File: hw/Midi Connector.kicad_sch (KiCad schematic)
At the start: 18 parts, among them J2 Midi In, J3 Midi Out, J4 Midi Thru, U5 74HC14, U6 H11L1

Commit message: huge schematic rework
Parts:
- removed C21, C22: 100n, Capacitor_SMD:C_0603_1608Metric, symbol Device:C
- removed D3: 1N4148WS, Diode_SMD:D_SOD-323, symbol Diode:1N4148WS
- removed J2: Midi In, DIN5_MIDI_MultiGround:DIN5_MIDI_MultiGround, symbol Connector:DIN-5_180degree
- removed J4: Midi Thru, DIN5_MIDI_MultiGround:DIN5_MIDI_MultiGround, symbol Connector:DIN-5_180degree
- removed R10, R15, R16: 220, Resistor_SMD:R_0603_1608Metric, symbol Device:R
- removed R11, R12: 1k, Resistor_SMD:R_0603_1608Metric, symbol Device:R
- removed TP6: MIDI_RX, TestPoint:TestPoint_Pad_D2.0mm, symbol Connector:TestPoint
- removed U6: H11L1, SOP-6-2.54mm:SOP-6_6.35x8.51mm_P02.54mm, symbol Isolator:H11L1
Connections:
- net STM_USART1_RX is gone; now on net GND: U5.11
- net GND: now also U5.9
- net at U5.10: no longer U5.9
- no-connect marks 10 -> 7
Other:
- moved on the sheet: C20, J3, R13, R14, TP7, U5A, U5B, U5C, U5D, U5E, U5F, U5G

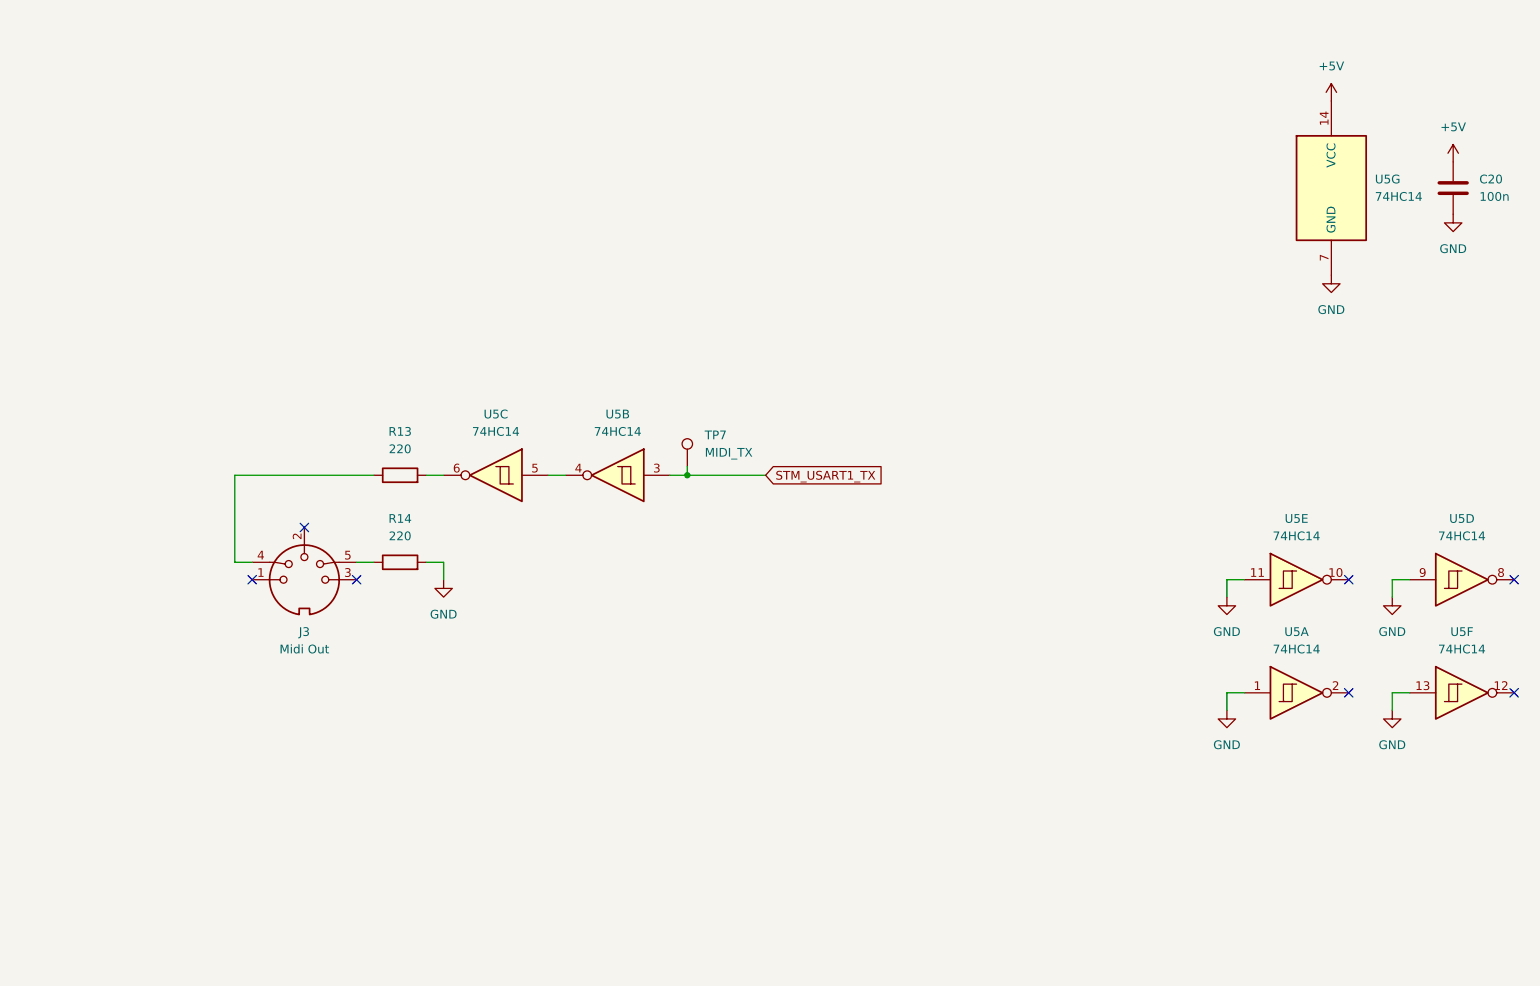
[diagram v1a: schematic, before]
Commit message: added new pcb design, ERC errors not fixed yet
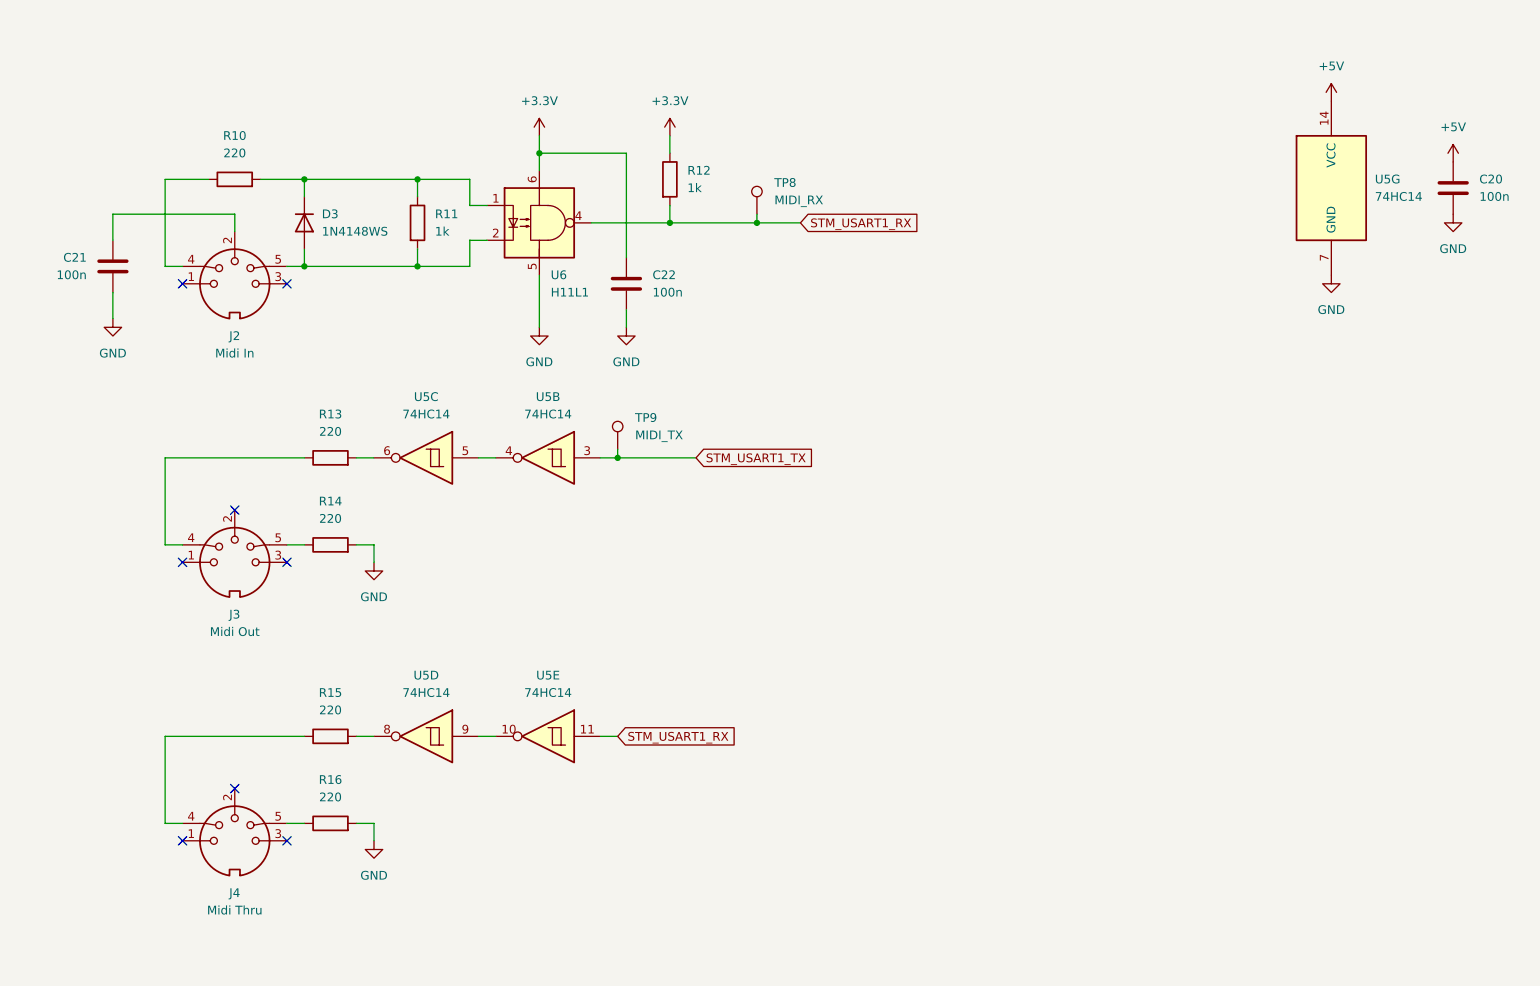
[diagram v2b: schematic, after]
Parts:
- removed unit 6 of U5
- removed unit 1 of U5
- added C21, C22: 100n, Capacitor_SMD:C_0603_1608Metric, symbol Device:C
- added D3: 1N4148WS, Diode_SMD:D_SOD-323, symbol Diode:1N4148WS
- added J2: Midi In, DIN5_MIDI_MultiGround:DIN5_MIDI_MultiGround, symbol Connector:DIN-5_180degree
- added J4: Midi Thru, DIN5_MIDI_MultiGround:DIN5_MIDI_MultiGround, symbol Connector:DIN-5_180degree
- added R10, R15, R16: 220, Resistor_SMD:R_0603_1608Metric, symbol Device:R
- added R11, R12: 1k, Resistor_SMD:R_0603_1608Metric, symbol Device:R
- added TP8: MIDI_RX, TestPoint:TestPoint_Pad_D2.0mm, symbol Connector:TestPoint
- added U6: H11L1, SOP-6-2.54mm:SOP-6_6.35x8.51mm_P02.54mm, symbol Isolator:H11L1
- renumbered TP7 to TP9
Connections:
- net GND: now also C21.2, C22.2, R16.2, U6.5; no longer U5.11, U5.9
- net at U5.8: now also R15.2
- net at U5.10: now also U5.9
- new net: J4.4, R15.1
- new net: J4.5, R16.1
- new net: D3.1 (K), R10.2, R11.1, U6.1
- new net: D3.2 (A), J2.5, R11.2, U6.2
- new net: C21.1, J2.2
- new net: J2.4, R10.1
- new net +3.3V: C22.1, R12.1, U6.6
- new net STM_USART1_RX: R12.2, TP8.1, U5.11, U6.4
- no-connect marks 7 -> 8
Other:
- moved on the sheet: J3, R13, R14, TP9, U5B, U5C

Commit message: updates to hardware layer
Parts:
- added C28: 100n, Capacitor_SMD:C_0603_1608Metric, symbol Device:C
- added unit 6 of U5
- added unit 1 of U5
- J2, J3, J4: symbol Connector:DIN-5_180degree -> Midi_Expressor:DIN-5_180degree_shielded
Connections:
- net GND: now also J3.S, J4.S, C28.2, U5.1, U5.13
- new net MIDI_IN_SHIELD: C28.1, J2.S
- no-connect marks 8 -> 10
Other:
- moved on the sheet: C21, C22, D3, R10, R11, R12, R13, R14, R15, R16, TP8, TP9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

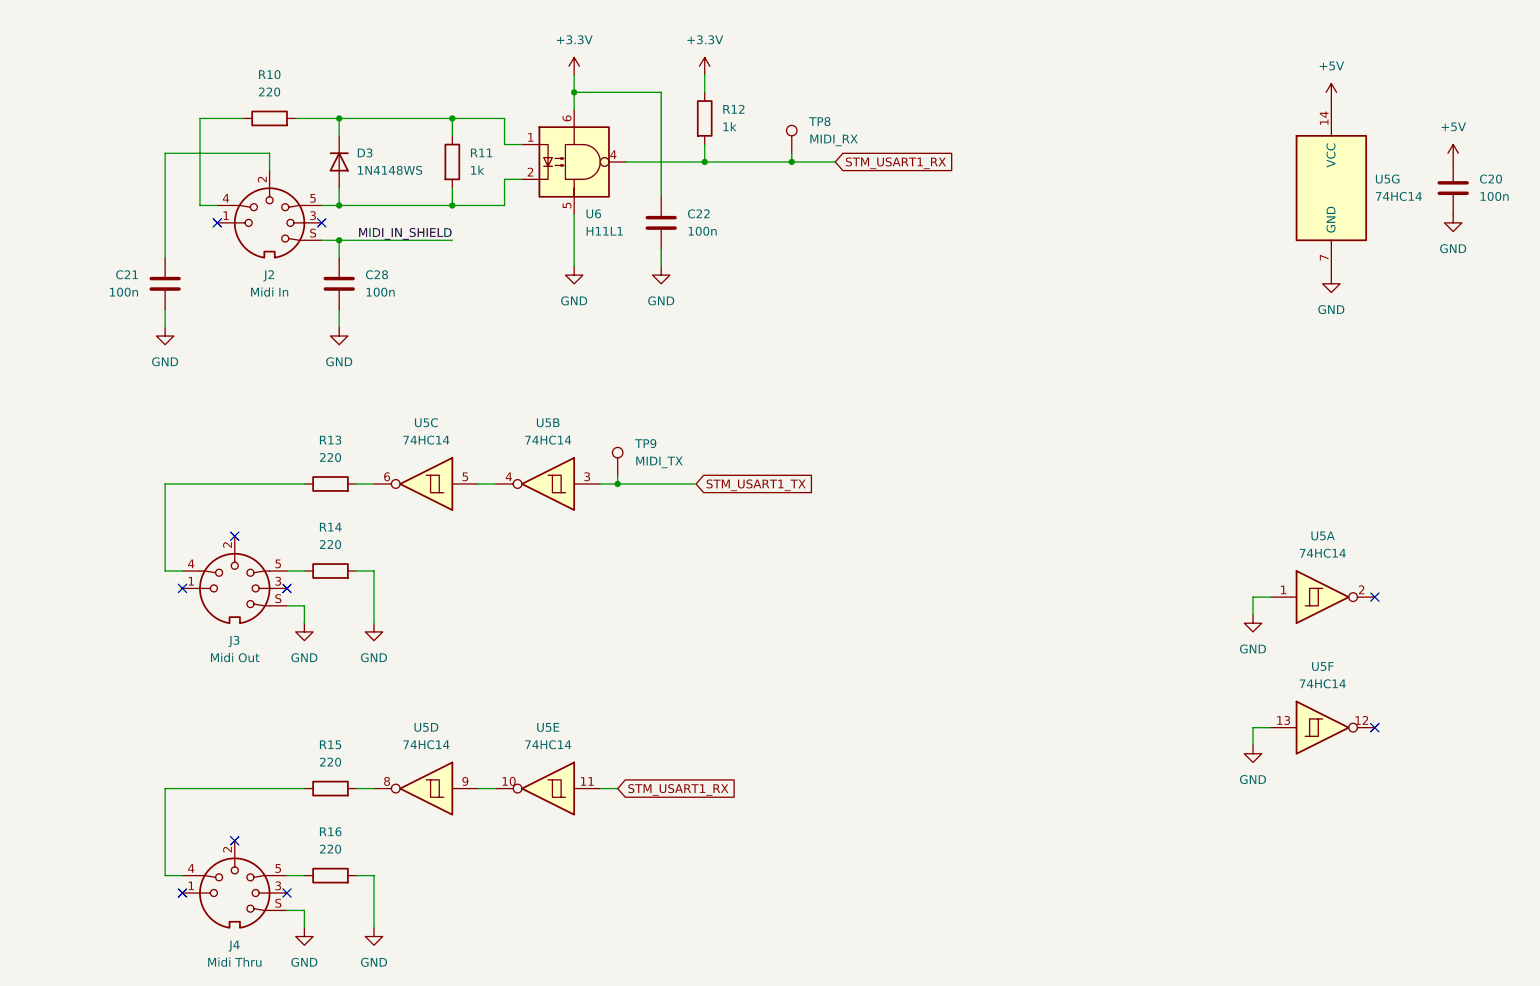
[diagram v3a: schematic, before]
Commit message: updated midi circuit to use 3.3V logic level
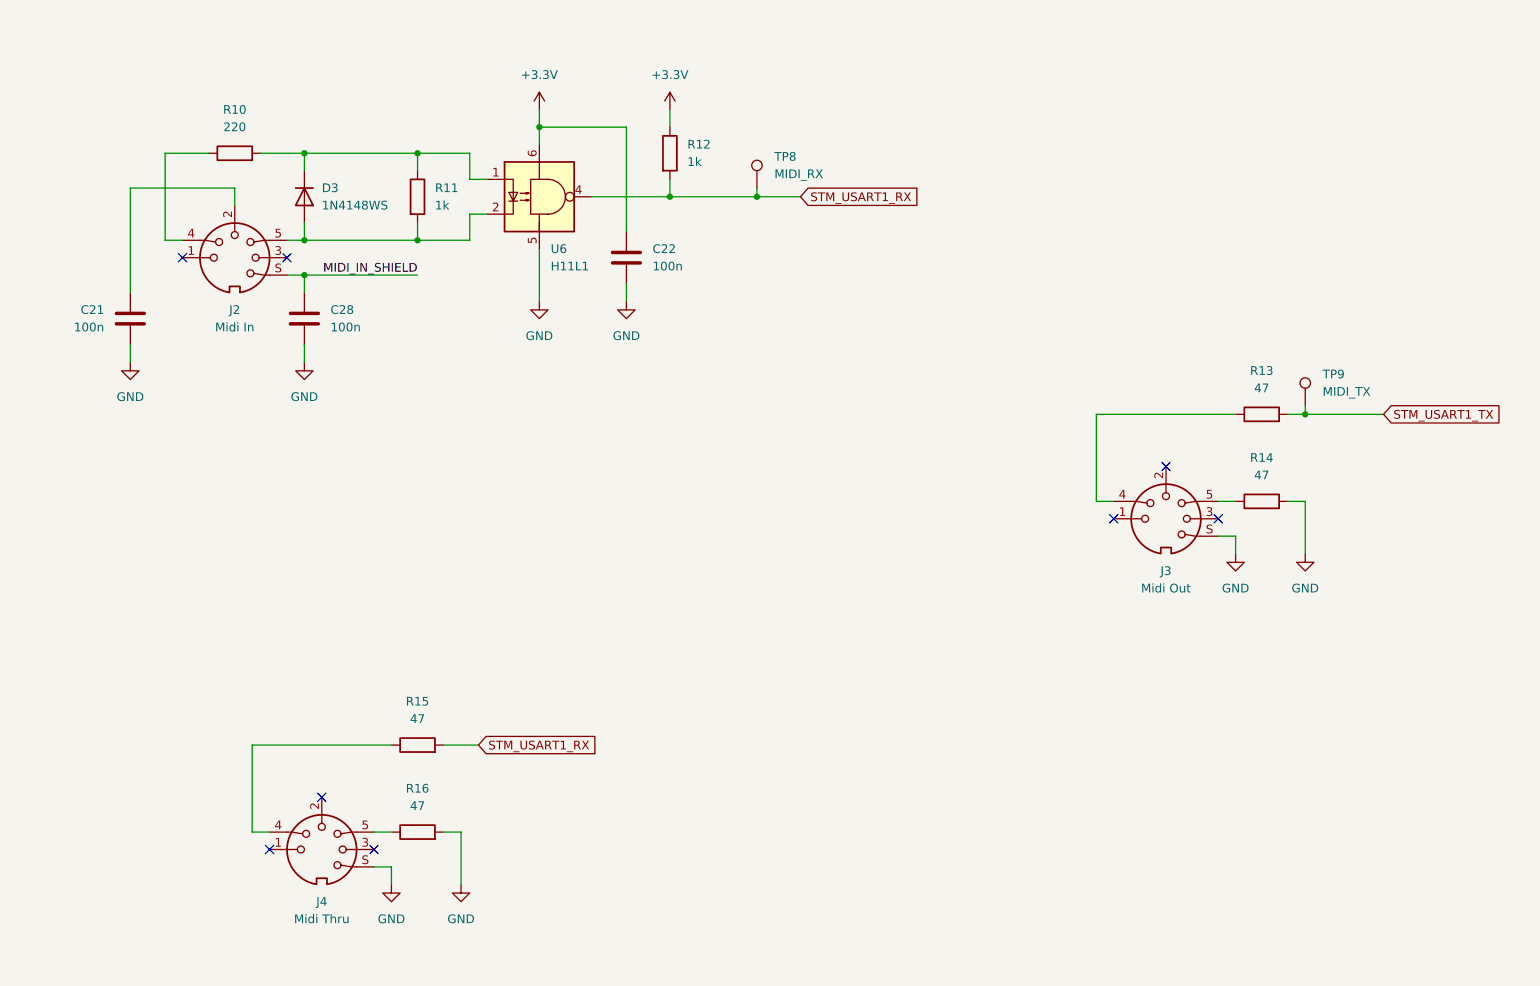
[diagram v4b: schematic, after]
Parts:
- removed C20: 100n, Capacitor_SMD:C_0603_1608Metric, symbol Device:C
- removed U5: 74HC14, Package_SO:SOIC-14_3.9x8.7mm_P1.27mm, symbol 74xx:74HC14
- R13, R14, R15, R16: value 220 -> 47; LCSC C22962 -> (none)
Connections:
- net STM_USART1_RX: now also R15.2
- net STM_USART1_TX: now also R13.2
- no-connect marks 10 -> 8
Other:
- moved on the sheet: C21, C22, C28, D3, J2, J3, J4, R10, R11, R12, R13, R14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

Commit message: removed MIDI Thru and updated Connector positioning
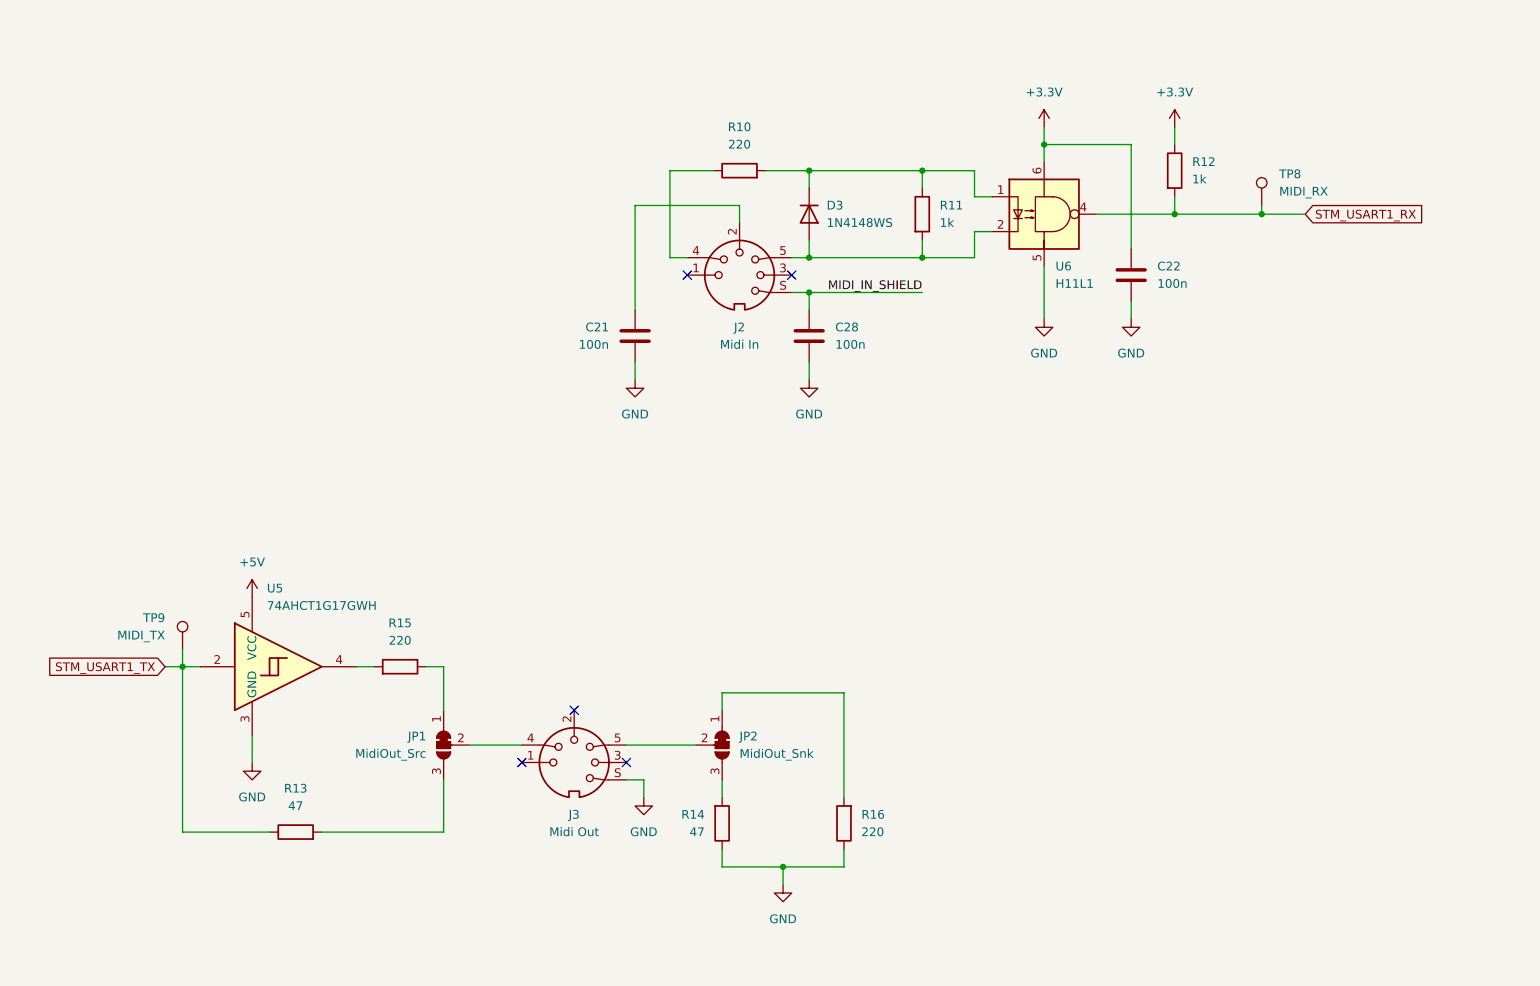
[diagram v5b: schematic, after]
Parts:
- removed J4: Midi Thru, DIN5_MIDI_MultiGround:DIN5_MIDI_MultiGround, symbol Midi_Expressor:DIN-5_180degree_shielded
- added JP1: MidiOut_Src, Jumper:SolderJumper-3_P1.3mm_Bridged12_RoundedPad1.0x1.5mm, symbol Jumper:SolderJumper_3_Bridged12
- added JP2: MidiOut_Snk, Jumper:SolderJumper-3_P1.3mm_Bridged12_RoundedPad1.0x1.5mm, symbol Jumper:SolderJumper_3_Bridged12
- added U5: 74AHCT1G17GWH, Package_TO_SOT_SMD:SOT-353_SC-70-5, symbol Midi_Expressor:74AHCT1G17GWH
- R13, R14: LCSC (none) -> C23182
- R15, R16: value 47 -> 220; LCSC (none) -> C22962
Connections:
- net GND: now also R14.1, R16.1, U5.3 (GND); no longer R14.2, R16.2
- net STM_USART1_RX: no longer R15.2
- net STM_USART1_TX: now also R13.1, U5.2; no longer R13.2
- net at R15.1: now also JP1.1 (A)
- net at J3.4: now also JP1.2 (C); no longer R13.1
- net at J3.5: now also JP2.2 (C); no longer R14.1
- new net: R15.2, U5.4
- new net: JP1.3 (B), R13.2
- new net: JP2.1 (A), R16.2
- new net: JP2.3 (B), R14.2
- new net +5V: U5.5 (VCC)
- no-connect marks 8 -> 5
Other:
- moved on the sheet: C21, C22, C28, D3, J2, J3, R10, R11, R12, R13, R14, TP8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

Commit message: added final production files for version 2
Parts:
- U5: LCSC (none) -> C554579
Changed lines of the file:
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@@
+			)
+		)
+		(property "LCSC" "C554579"
+			(at 71.9933 116.84 0)
+			(effects
+				(font
+					(size 1.27 1.27)
+				)
+				(hide yes)
 			)
 		)
